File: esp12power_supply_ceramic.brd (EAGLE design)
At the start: 31.5 x 30 mm, 16 parts, among them J1 1X2-3.5MM, J2 1X2-3.5MM, J3 1X2-3.5MM

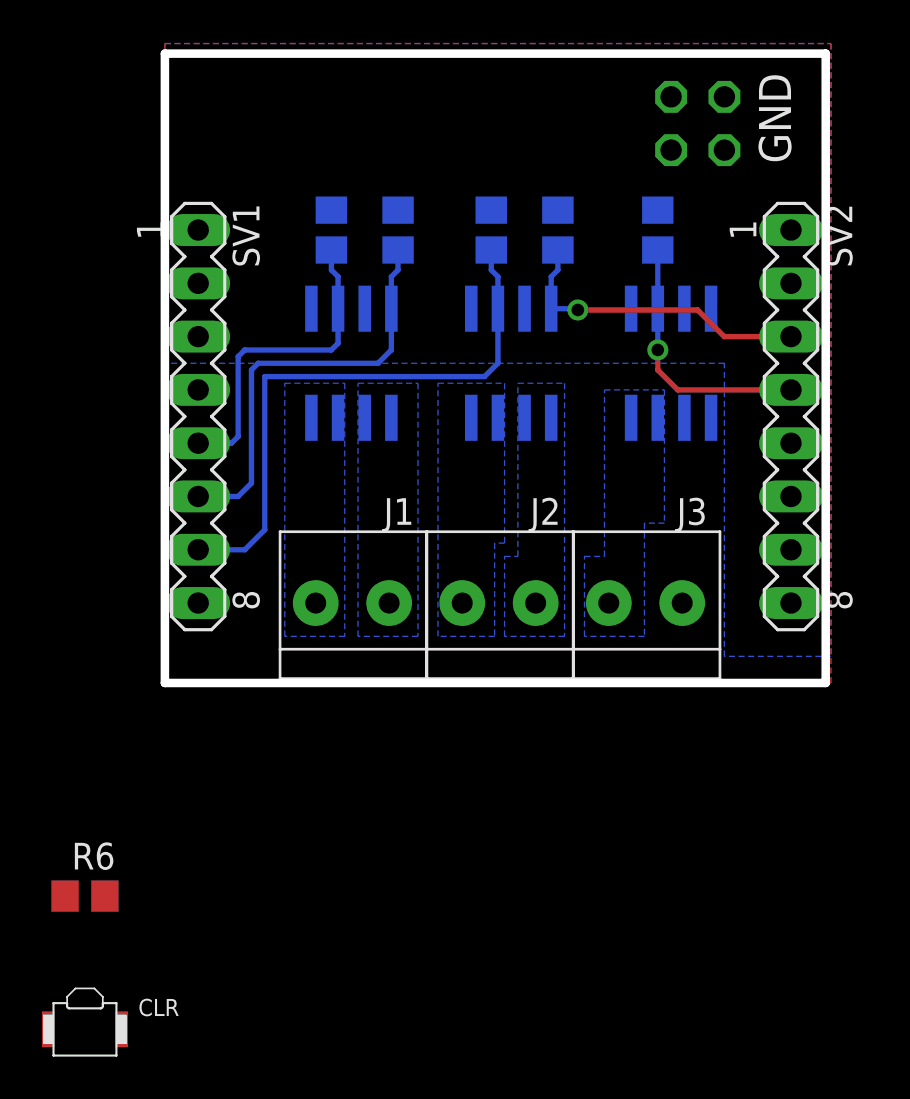
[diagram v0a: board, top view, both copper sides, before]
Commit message: added an ftdi version
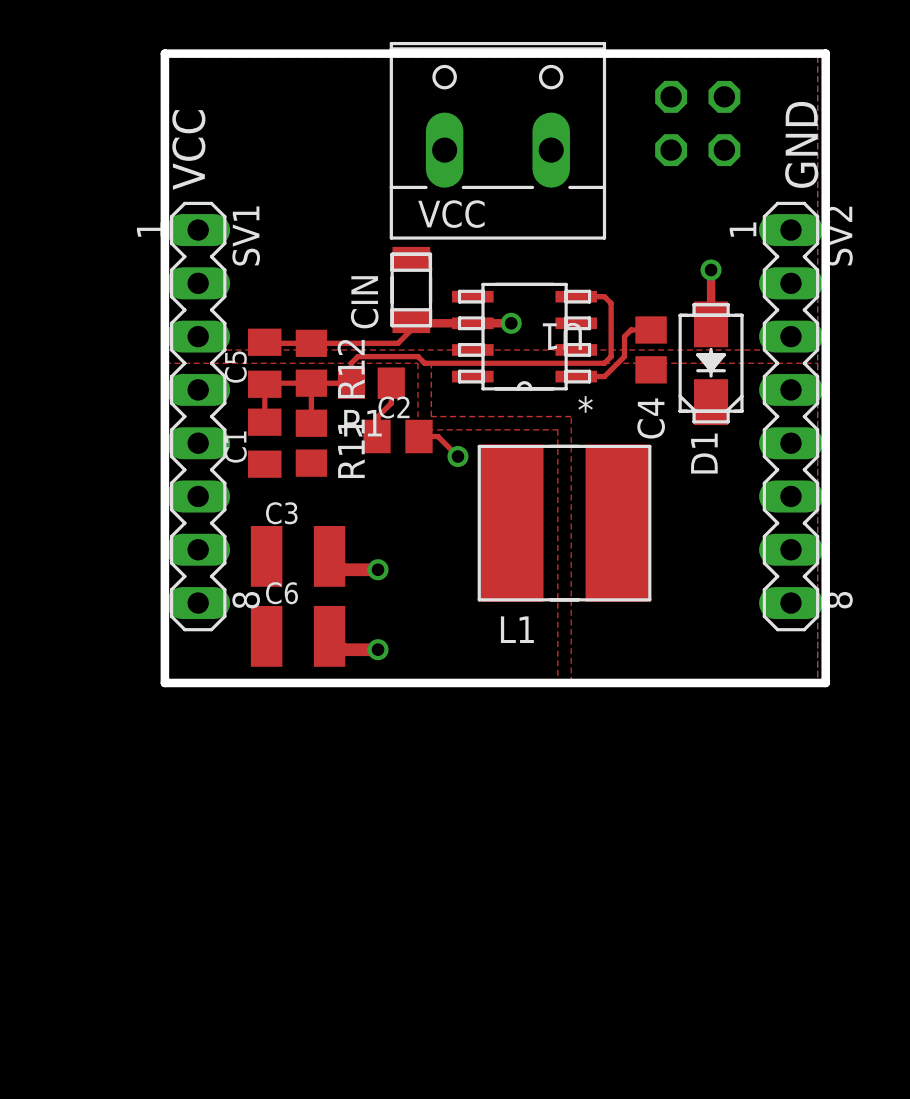
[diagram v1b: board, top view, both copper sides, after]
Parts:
- removed CLR: SPST.B3U-3000P(M), omron:B3U-3000P(M)
- removed J1, J2, J3: 1X2-3.5MM, adafruit:1X2-3.5MM
- removed R2, R3, R4, R5, R6: 10k, rcl:R0805
- removed U$1, U$2, U$3: AOD4806, esp12_RGBWW:SO08
- added C1: 2.7nF, esp12_RGBWW:C0805K
- added C2: 56nF, esp12_RGBWW:C0805K
- added C3, C6: 45µ, esp12_RGBWW:C1210K
- added C4: 10nF, resistor:C0805
- added C5: 150pF, esp12_RGBWW:C0805K
- added CIN: 4.7uF, AcceleratedDesigns_Lib:1206
- added D1: 570mV, TI_Accelerated_Design_neu:SMA
- added L1: 68uH, AcceleratedDesigns_Lib:IND_NPI75C
- added R11: 10k, resistor:R0805
- added R12: 3.24k, resistor:R0805
- added U1: TPS5410DR, AcceleratedDesigns_Lib:M08A
- added VCC: (no value), con-wago-508:W237-132
- R1: value 10k -> 1.78k; device rcl:R0805 -> resistor:R0805
- moved R1 15.5 mm to (9.84, 14.3), flipped to the top, turned to 180 degrees
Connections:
- removed net ADC: SV1.2
- removed net B: J1.2, U$1.7, U$1.8
- removed net CH_PD: SV1.3
- removed net CW: J2.1, U$2.5, U$2.6
- removed net G: J1.1, U$1.5, U$1.6
- removed net GPIO0: SV2.5
- removed net GPIO12: R4.1, SV1.6, U$1.4
- removed net GPIO13: R5.1, SV1.7, U$2.2
- removed net GPIO14: R3.1, SV1.5, U$1.2
- removed net GPIO15: SV2.7
- removed net GPIO16: CLR.2, R6.1, SV1.4
- removed net GPIO2: SV2.6
- removed net GPIO4: R1.2, SV2.4, U$3.2
- removed net GPIO5: R2.1, SV2.3, U$2.4
- removed net R: J2.2, U$2.7, U$2.8
- removed net REST: SV1.1
- removed net RXD: SV2.2
- removed net TXD: SV2.1
- removed net VCC: CLR.1, SV1.8
- removed net WW: J3.2, U$3.7, U$3.8
- new net +3V3: C1.1, C3.1, C6.1, L1.1, R11.2, SV1.8
- new net BOOT: C4.1, U1.1
- new net N$1: C2.1, R1.1
- new net PH: C4.2, D1.1, L1.2, U1.8
- new net VSNS: C1.2, C5.1, R1.2, R11.1, R12.2, U1.4
- net +12V: now also CIN.2, U1.7, VCC.1; no longer J3.1
- net GND: now also C2.2, C3.2, C5.2, C6.2, CIN.1, D1.2, R12.1, U1.6, VCC.2; no longer R1.1, R2.2, R3.2, R4.2, R5.2, R6.2, U$1.1, U$1.3, U$2.1, U$2.3, U$3.1
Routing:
- net GPIO13: track 27.8 -> 0.00 mm
- net VSNS: track 0.00 -> 25.9 mm
- net GND: track 0.00 -> 22.5 mm, vias 0 -> 5
- net GPIO12: track 20.2 -> 0.00 mm
- net GPIO14: track 15.5 -> 0.00 mm
- net GPIO5: track 14.9 -> 0.00 mm, vias 1 -> 0
- net GPIO4: track 12.5 -> 0.00 mm, vias 1 -> 0
- net BOOT: track 0.00 -> 5.05 mm
- net N$1: track 0.00 -> 2.82 mm
- added copper zone on layer 1, net +3V3
- added copper zone on layer 1, net PH
- removed copper zone on layer 16, net B
- removed copper zone on layer 16, net CW
- removed copper zone on layer 16, net G
- removed copper zone on layer 16, net R
- removed copper zone on layer 16, net WW
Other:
- board text added: "VCC"
